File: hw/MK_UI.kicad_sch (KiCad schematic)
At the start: 35 parts, among them J11 Conn_01x03, J16 UI 20-Ribbon, J2 Conn_01x20, J3 SW_MATRIX, SW2 UP, SW3 RT, SW4 DN, SW5 LF, SW6 EN

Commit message: UI PCB initial
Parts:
- C10, C11, C12, C7, C8, C9, CF1, CF2: footprint (none) -> Capacitor_THT:C_Axial_L5.1mm_D3.1mm_P7.50mm_Horizontal
- DISP-1: value ~ -> TFT-SPI w/Touch 9/5; footprint (none) -> Connector_PinSocket_2.54mm:PinSocket_1x14_P2.54mm_Vertical
- H1, H2, H3, H4, M_DISP1, M_DISP2, M_DISP3: footprint MountingHole:MountingHole_2.7mm_M2.5 -> MountingHole:MountingHole_3.2mm_M3
- J11: footprint (none) -> Connector_PinSocket_2.54mm:PinSocket_1x03_P2.54mm_Vertical
- J16: footprint (none) -> Connector_PinHeader_2.54mm:PinHeader_2x10_P2.54mm_Vertical
- J2: value Conn_01x20 -> Conn_01x20-FFC; footprint (none) -> AES_Library:Amphenol_F51L_1x20_P1.00mm_Horizontal-FFC
- J3: value SW_MATRIX -> SW_MATRIX-Conn; footprint (none) -> Connector_PinHeader_2.54mm:PinHeader_1x05_P2.54mm_Vertical
- R3, R4, R5, R6, R7: footprint (none) -> Resistor_THT:R_Axial_DIN0207_L6.3mm_D2.5mm_P10.16mm_Horizontal
- RE1: value RotaryEncoder_Switch -> RotEnc-SW; footprint (none) -> Rotary_Encoder:RotaryEncoder_Bourns_Vertical_PEC12R-3xxxF-Sxxxx
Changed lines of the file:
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@@
       (effects (font (size 1.27 1.27)) (justify right))
     )
-    (property "Footprint" "" (at 87.376 186.436 90)
+    (property "Footprint" "Resistor_THT:R_Axial_DIN0207_L6.3mm_D2.5mm_P10.16mm_Horizontal" (at 87.376 186.436 90)
       (effects (font (size 1.27 1.27)) hide)
     )
@@
       (effects (font (size 1.27 1.27)) (justify left))
     )
-    (property "Footprint" "MountingHole:MountingHole_2.7mm_M2.5" (at 212.09 76.2 0)
+    (property "Footprint" "MountingHole:MountingHole_3.2mm_M3" (at 212.09 76.2 0)
       (effects (font (size 1.27 1.27)) hide)
     )
@@
       (effects (font (size 1.27 1.27)) (justify left))
     )
-    (property "Footprint" "MountingHole:MountingHole_2.7mm_M2.5" (at 245.11 154.94 0)
+    (property "Footprint" "MountingHole:MountingHole_3.2mm_M3" (at 245.11 154.94 0)
       (effects (font (size 1.27 1.27)) hide)
     )
@@
       (effects (font (size 1.27 1.27)) (justify left))
     )
-    (property "Footprint" "" (at 49.53 38.1 0)
+    (property "Footprint" "Capacitor_THT:C_Axial_L5.1mm_D3.1mm_P7.50mm_Horizontal" (at 49.53 38.1 0)
       (effects (font (size 1.27 1.27)) hide)
     )
@@
       (effects (font (size 1.27 1.27)) (justify left))
     )
-    (property "Footprint" "MountingHole:MountingHole_2.7mm_M2.5" (at 245.11 149.86 0)
+    (property "Footprint" "MountingHole:MountingHole_3.2mm_M3" (at 245.11 149.86 0)
       (effects (font (size 1.27 1.27)) hide)
     )
@@
       (effects (font (size 1.27 1.27)) (justify left))
     )
-    (property "Footprint" "" (at 38.1 38.1 0)
+    (property "Footprint" "Capacitor_THT:C_Axial_L5.1mm_D3.1mm_P7.50mm_Horizontal" (at 38.1 38.1 0)
       (effects (font (size 1.27 1.27)) hide)
     )
@@
       (effects (font (size 1.27 1.27)))
     )
-    (property "Value" "RotaryEncoder_Switch" (at 102.87 152.4 0)
-      (effects (font (size 1.27 1.27)) hide)
-    )
-    (property "Footprint" "" (at 99.06 150.114 0)
+    (property "Value" "RotEnc-SW" (at 102.87 152.4 0)
+      (effects (font (size 1.27 1.27)) hide)
+    )
+    (property "Footprint" "Rotary_Encoder:RotaryEncoder_Bourns_Vertical_PEC12R-3xxxF-Sxxxx" (at 99.06 150.114 0)
       (effects (font (size 1.27 1.27)) hide)
     )
@@
       (effects (font (size 1.27 1.27)))
     )
-    (property "Footprint" "" (at 78.74 176.53 0)
+    (property "Footprint" "Capacitor_THT:C_Axial_L5.1mm_D3.1mm_P7.50mm_Horizontal" (at 78.74 176.53 0)
       (effects (font (size 1.27 1.27)) hide)
     )
@@
       (effects (font (size 1.27 1.27)))
     )
-    (property "Footprint" "" (at 102.87 176.53 0)
+    (property "Footprint" "Capacitor_THT:C_Axial_L5.1mm_D3.1mm_P7.50mm_Horizontal" (at 102.87 176.53 0)
       (effects (font (size 1.27 1.27)) hide)
     )
@@
       (effects (font (size 1.27 1.27)) (justify left))
     )
-    (property "Footprint" "" (at 119.38 146.05 0)
+    (property "Footprint" "Capacitor_THT:C_Axial_L5.1mm_D3.1mm_P7.50mm_Horizontal" (at 119.38 146.05 0)
       (effects (font (size 1.27 1.27)) hide)
     )
@@
       (effects (font (size 1.27 1.27)) (justify left))
     )
-    (property "Value" "~" (at 195.77 44.45 0)
-      (effects (font (size 1.27 1.27)))
-    )
-    (property "Footprint" "" (at 195.77 44.45 0)
+    (property "Value" "TFT-SPI w/Touch 9/5" (at 195.77 44.45 0)
+      (effects (font (size 1.27 1.27)) hide)
+    )
+    (property "Footprint" "Connector_PinSocket_2.54mm:PinSocket_1x14_P2.54mm_Vertical" (at 195.77 44.45 0)
       (effects (font (size 1.27 1.27)) hide)
     )
@@
       (effects (font (size 1.27 1.27)) hide)
     )
-    (property "Footprint" "" (at 212.09 36.83 0)
+    (property "Footprint" "Connector_PinSocket_2.54mm:PinSocket_1x03_P2.54mm_Vertical" (at 212.09 36.83 0)
       (effects (font (size 1.27 1.27)) hide)
     )
@@
       (effects (font (size 1.27 1.27)) (justify left))
     )
-    (property "Footprint" "MountingHole:MountingHole_2.7mm_M2.5" (at 245.11 144.78 0)
+    (property "Footprint" "MountingHole:MountingHole_3.2mm_M3" (at 245.11 144.78 0)
       (effects (font (size 1.27 1.27)) hide)
     )
@@
       (effects (font (size 1.27 1.27)) (justify left))
     )
-    (property "Footprint" "" (at 120.396 132.334 90)
+    (property "Footprint" "Resistor_THT:R_Axial_DIN0207_L6.3mm_D2.5mm_P10.16mm_Horizontal" (at 120.396 132.334 90)
       (effects (font (size 1.27 1.27)) hide)
     )
@@
       (effects (font (size 1.27 1.27)) (justify left))
     )
-    (property "Footprint" "MountingHole:MountingHole_2.7mm_M2.5" (at 245.11 160.02 0)
+    (property "Footprint" "MountingHole:MountingHole_3.2mm_M3" (at 245.11 160.02 0)
       (effects (font (size 1.27 1.27)) hide)
     )
@@
       (effects (font (size 1.27 1.27)) (justify right))
     )
-    (property "Footprint" "" (at 63.246 173.736 90)
+    (property "Footprint" "Resistor_THT:R_Axial_DIN0207_L6.3mm_D2.5mm_P10.16mm_Horizontal" (at 63.246 173.736 90)
       (effects (font (size 1.27 1.27)) hide)
     )
@@
       (effects (font (size 1.27 1.27)))
     )
-    (property "Value" "SW_MATRIX" (at 22.86 147.32 0)
-      (effects (font (size 1.27 1.27)))
-    )
-    (property "Footprint" "" (at 22.86 139.7 0)
+    (property "Value" "SW_MATRIX-Conn" (at 22.86 147.32 0)
+      (effects (font (size 1.27 1.27)))
+    )
+    (property "Footprint" "Connector_PinHeader_2.54mm:PinHeader_1x05_P2.54mm_Vertical" (at 22.86 139.7 0)
       (effects (font (size 1.27 1.27)) hide)
     )
@@
       (effects (font (size 1.27 1.27)) (justify left))
     )
-    (property "Footprint" "MountingHole:MountingHole_2.7mm_M2.5" (at 212.09 66.04 0)
+    (property "Footprint" "MountingHole:MountingHole_3.2mm_M3" (at 212.09 66.04 0)
       (effects (font (size 1.27 1.27)) hide)
     )
@@
       (effects (font (size 1.27 1.27)) (justify right))
     )
-    (property "Footprint" "" (at 87.376 173.736 90)
+    (property "Footprint" "Resistor_THT:R_Axial_DIN0207_L6.3mm_D2.5mm_P10.16mm_Horizontal" (at 87.376 173.736 90)
       (effects (font (size 1.27 1.27)) hide)
     )
@@
       (effects (font (size 1.27 1.27)) (justify left))
     )
-    (property "Footprint" "MountingHole:MountingHole_2.7mm_M2.5" (at 212.09 71.12 0)
+    (property "Footprint" "MountingHole:MountingHole_3.2mm_M3" (at 212.09 71.12 0)
       (effects (font (size 1.27 1.27)) hide)
     )
@@
       (effects (font (size 1.27 1.27)) (justify left))
     )
-    (property "Value" "Conn_01x20" (at 25.4 58.42 0)
+    (property "Value" "Conn_01x20-FFC" (at 25.4 58.42 0)
       (effects (font (size 1.27 1.27)) (justify left) hide)
     )
-    (property "Footprint" "" (at 22.86 86.36 0)
+    (property "Footprint" "AES_Library:Amphenol_F51L_1x20_P1.00mm_Horizontal-FFC" (at 22.86 86.36 0)
       (effects (font (size 1.27 1.27)) hide)
     )
@@
       (effects (font (size 1.27 1.27)))
     )
-    (property "Footprint" "" (at 54.61 176.53 0)
+    (property "Footprint" "Capacitor_THT:C_Axial_L5.1mm_D3.1mm_P7.50mm_Horizontal" (at 54.61 176.53 0)
       (effects (font (size 1.27 1.27)) hide)
     )
@@
       (effects (font (size 1.27 1.27)) (justify right))
     )
-    (property "Footprint" "" (at 87.376 161.036 90)
+    (property "Footprint" "Resistor_THT:R_Axial_DIN0207_L6.3mm_D2.5mm_P10.16mm_Horizontal" (at 87.376 161.036 90)
       (effects (font (size 1.27 1.27)) hide)
     )
@@
       (effects (font (size 1.27 1.27)))
     )
-    (property "Footprint" "" (at 85.09 93.98 0)
+    (property "Footprint" "Connector_PinHeader_2.54mm:PinHeader_2x10_P2.54mm_Vertical" (at 85.09 93.98 0)
       (effects (font (size 1.27 1.27)) hide)
     )
@@
       (effects (font (size 1.27 1.27)) (justify right))
     )
-    (property "Footprint" "" (at 111.506 173.736 90)
+    (property "Footprint" "Resistor_THT:R_Axial_DIN0207_L6.3mm_D2.5mm_P10.16mm_Horizontal" (at 111.506 173.736 90)
       (effects (font (size 1.27 1.27)) hide)
     )
@@
       (effects (font (size 1.27 1.27)))
     )
-    (property "Footprint" "" (at 78.74 163.83 0)
+    (property "Footprint" "Capacitor_THT:C_Axial_L5.1mm_D3.1mm_P7.50mm_Horizontal" (at 78.74 163.83 0)
       (effects (font (size 1.27 1.27)) hide)
     )
@@
       (effects (font (size 1.27 1.27)))
     )
-    (property "Footprint" "" (at 78.74 189.23 0)
-      (effects (font (size 1.27 1.27)) hide)
-    )
+    (property "Footprint" "Capacitor_THT:C_Axial_L5.1mm_D3.1mm_P7.50mm_Horizontal" (at 78.74 189.23 0)
+      (effects (font (size 1.27 1.27)) hide)
+    )

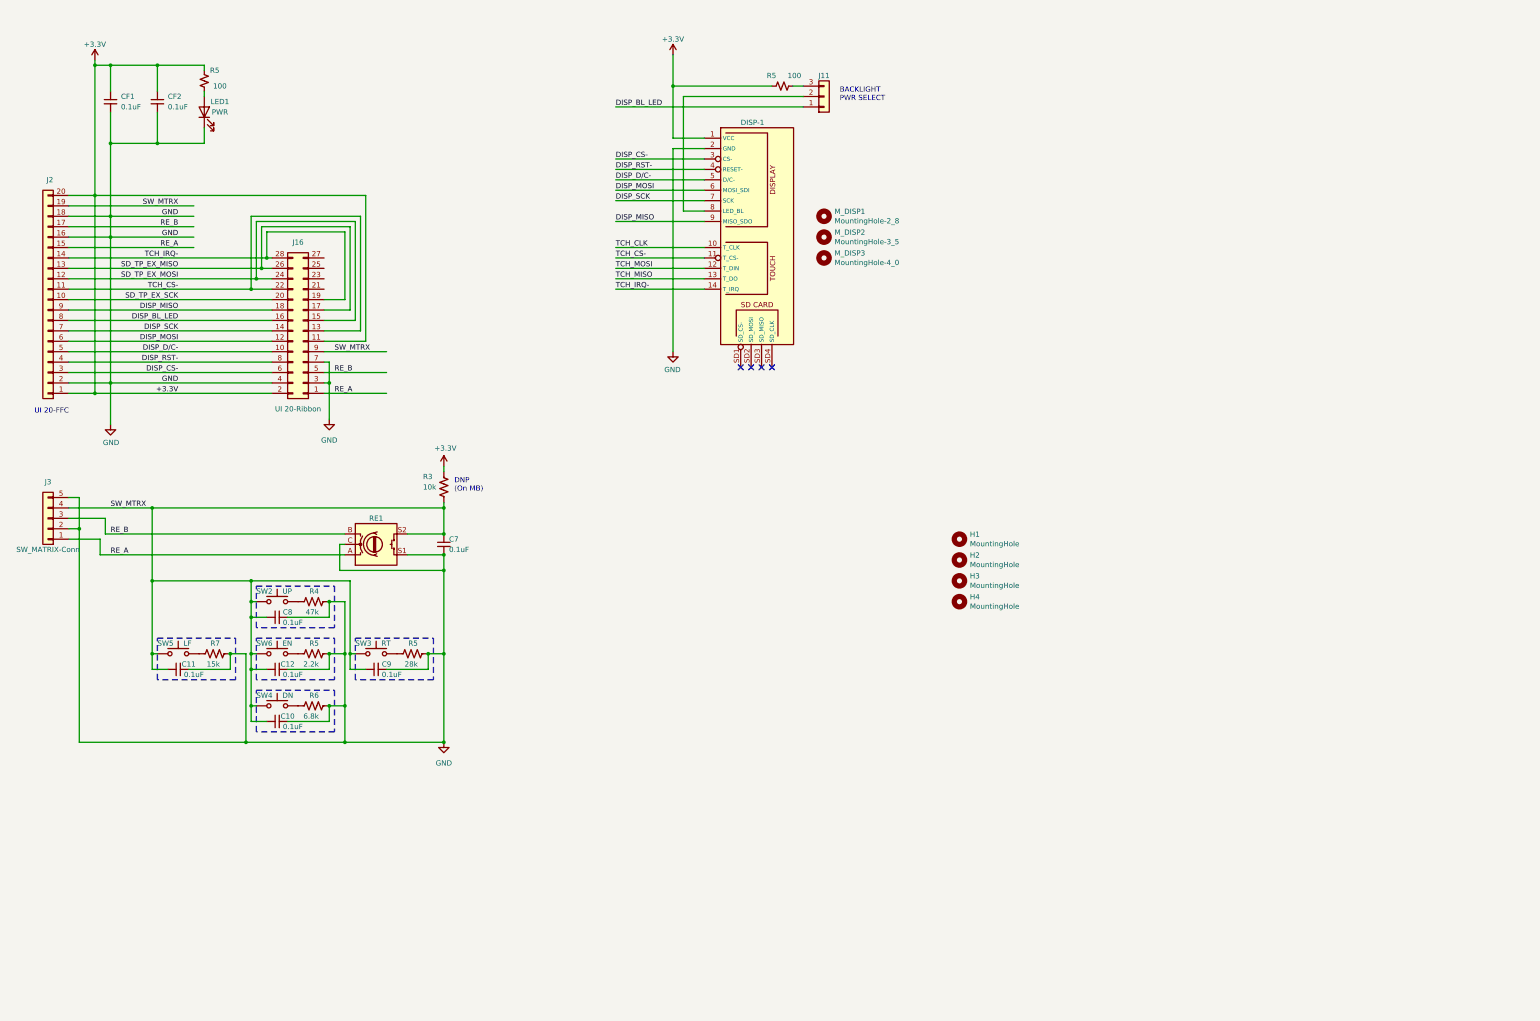
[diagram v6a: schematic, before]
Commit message: Device (Main) and K&S-IF ready for layout.
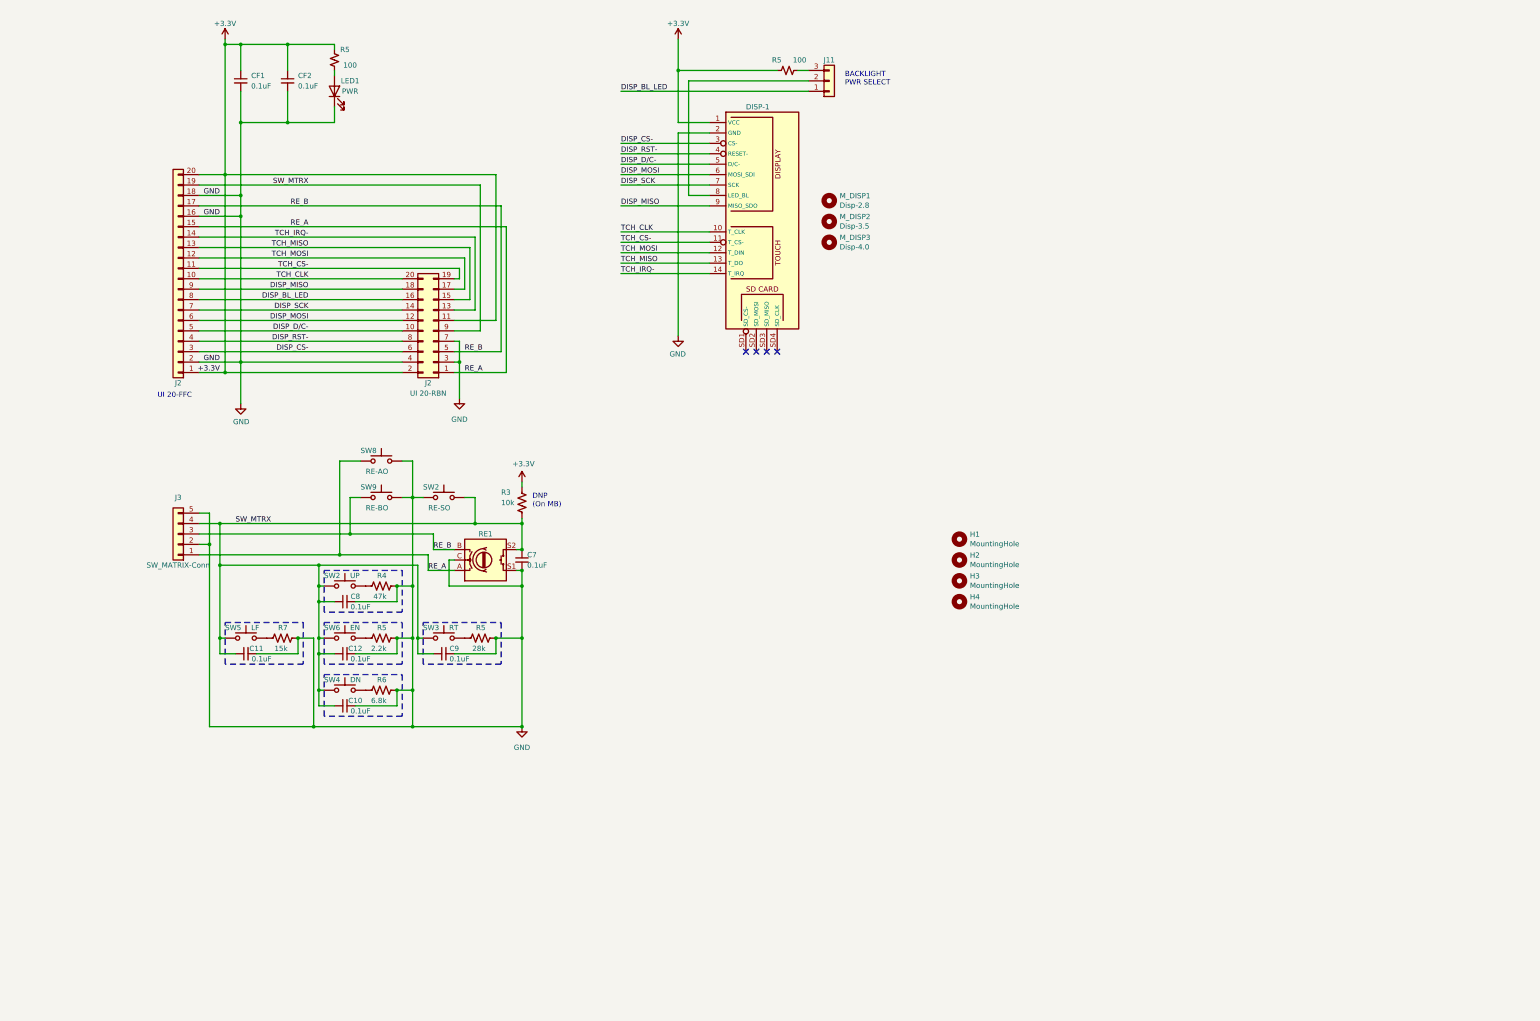
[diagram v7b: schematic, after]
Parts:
- removed J16: UI 20-Ribbon, Connector_PinHeader_2.54mm:PinHeader_2x10_P2.54mm_Vertical, symbol Connector_Generic:Conn_02x14_Odd_Even
- added J2: UI 20-RBN, Connector_PinHeader_2.54mm:PinHeader_2x10_P2.54mm_Vertical, symbol Connector_Generic:Conn_02x10_Odd_Even
- added SW2: RE-SO, AES_Library:SW_PUSH_SMD_1P1T_NO_45x45mm-CK, symbol Switch:SW_Push
- added SW8: RE-AO, AES_Library:SW_PUSH_SMD_1P1T_NO_45x45mm-CK, symbol Switch:SW_Push
- added SW9: RE-BO, AES_Library:SW_PUSH_SMD_1P1T_NO_45x45mm-CK, symbol Switch:SW_Push
- LED1: footprint LED_THT:LED_D5.0mm -> AES_Library:LED_SMD_SIDEVIEW_Harvatek
- M_DISP1: value MountingHole-2_8 -> Disp-2.8
- M_DISP2: value MountingHole-3_5 -> Disp-3.5
- M_DISP3: value MountingHole-4_0 -> Disp-4.0
- SW2, SW3, SW4, SW5, SW6: footprint Button_Switch_SMD:SW_Push_1P1T_NO_Vertical_Wuerth_434133025816 -> AES_Library:SW_PUSH_SMD_1P1T_NO_6x6mm
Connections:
- net SD_TP_EX_MISO is gone; now on net TCH_MISO: J2.13 (Pin_13)
- net SD_TP_EX_MOSI is gone; now on net TCH_MOSI: J2.12 (Pin_12)
- net SD_TP_EX_SCK is gone; now on net TCH_CLK: J2.10 (Pin_10)
- net +3.3V: now also J2.11 (Pin_11), J2.2 (Pin_2)
- net DISP_BL_LED: now also J2.16 (Pin_16)
- net DISP_CS-: now also J2.6 (Pin_6)
- net DISP_D/C-: now also J2.10 (Pin_10)
- net DISP_MISO: now also J2.18 (Pin_18)
- net DISP_MOSI: now also J2.12 (Pin_12)
- net DISP_RST-: now also J2.8 (Pin_8)
- net DISP_SCK: now also J2.14 (Pin_14)
- net GND: now also J2.3 (Pin_3), J2.4 (Pin_4), J2.7 (Pin_7), SW2.1, SW8.2, SW9.2
- net RE_A: now also J2.1 (Pin_1), SW8.1
- net RE_B: now also J2.5 (Pin_5), SW9.1
- net SW_MTRX: now also J2.9 (Pin_9), SW2.2
- net TCH_CLK: now also J2.20 (Pin_20)
- net TCH_CS-: now also J2.19 (Pin_19)
- net TCH_IRQ-: now also J2.13 (Pin_13)
- net TCH_MISO: now also J2.15 (Pin_15)
- net TCH_MOSI: now also J2.17 (Pin_17)
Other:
- moved on the sheet: C10, C11, C12, C7, C8, C9, CF1, CF2, DISP-1, J11, J2, J3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
